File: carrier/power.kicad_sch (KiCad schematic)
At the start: 10 parts

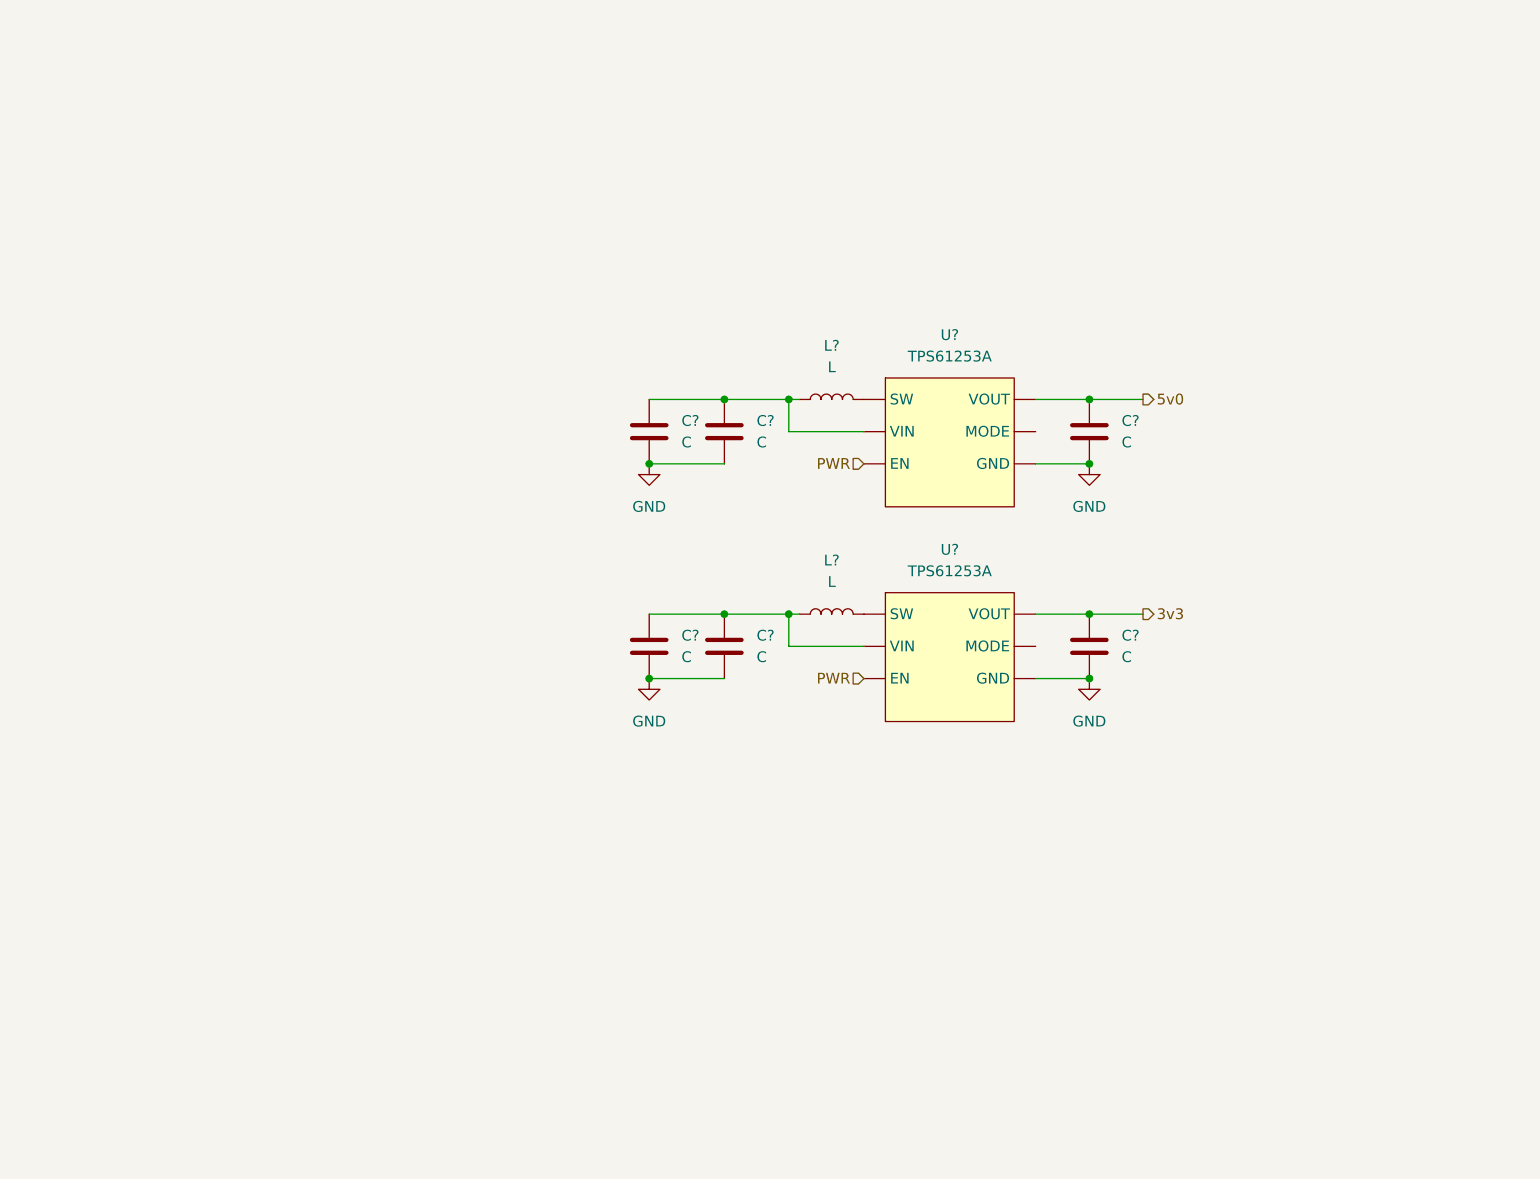
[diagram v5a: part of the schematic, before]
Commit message: add correct charge chip
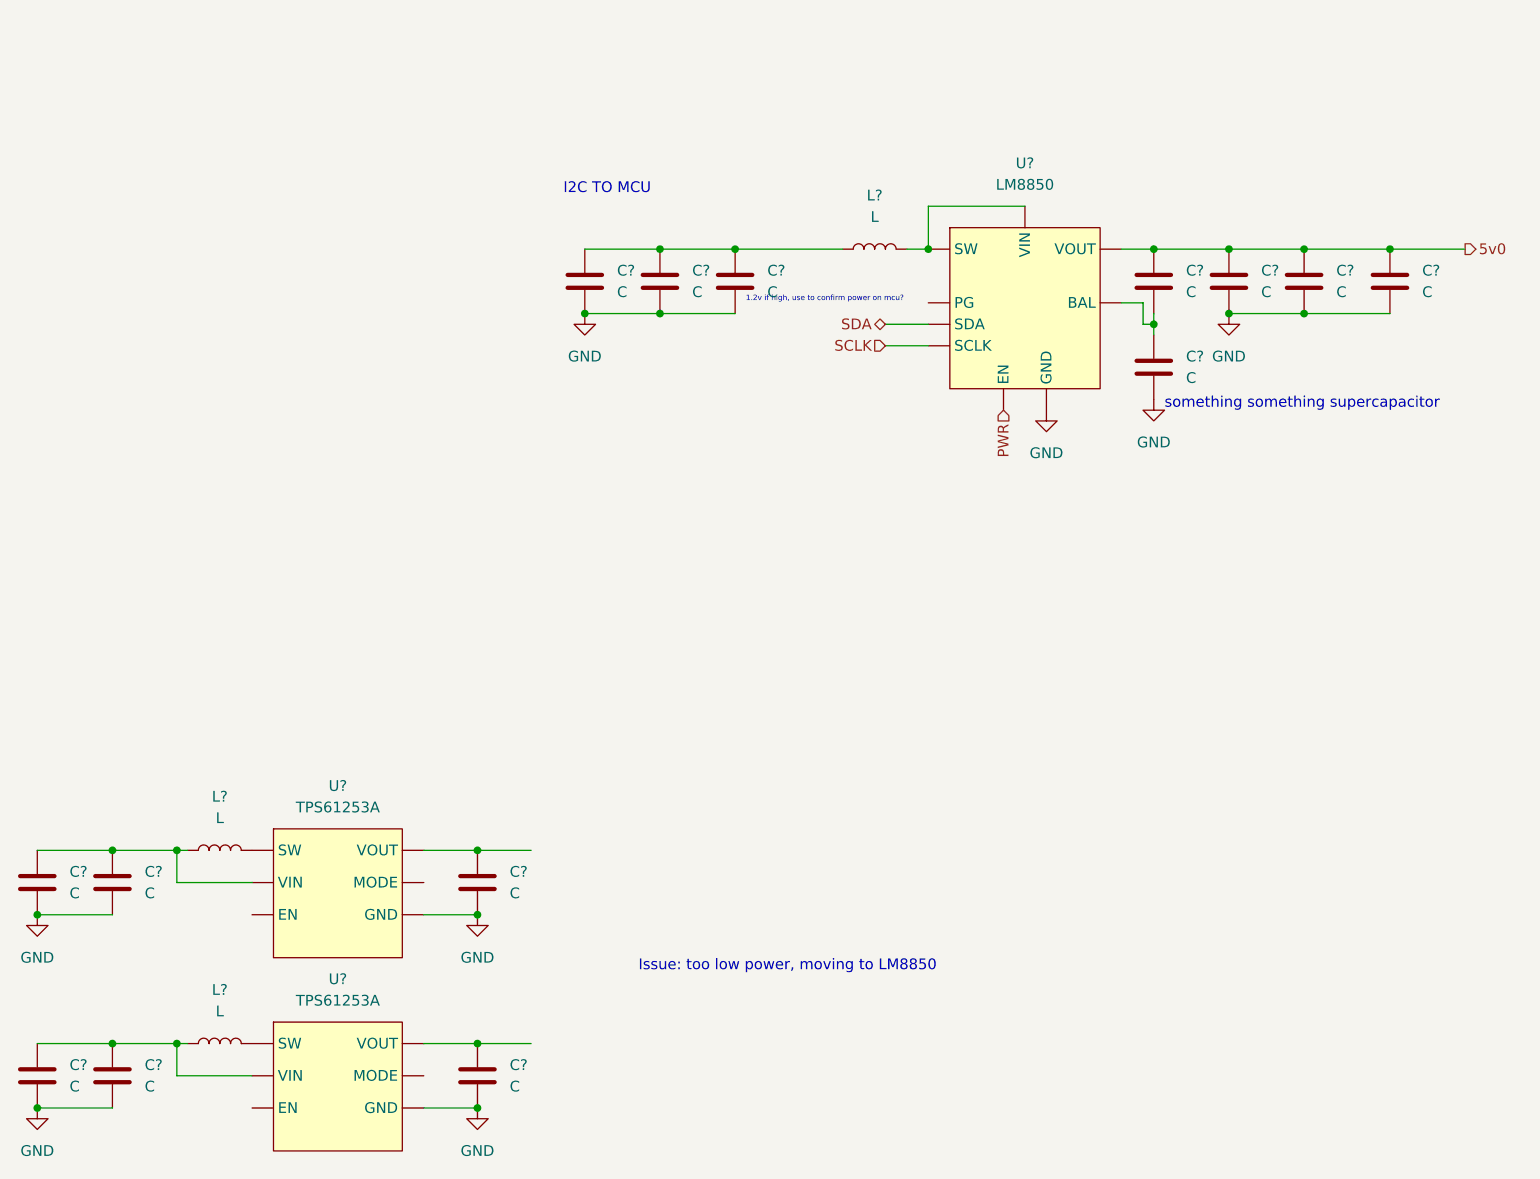
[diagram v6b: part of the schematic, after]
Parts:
- added C? (x8): C, symbol Device:C
- added L?: L, symbol Device:L
- added U?: LM8850, symbol CM4IO:LM8850
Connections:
- net 5v0: now also C?.1, C?.1, C?.1, C?.1, U?. (VOUT); no longer C?.1, U?. (VOUT)
- net GND: now also C?.2, C?.2, C?.2, C?.2, C?.2, C?.2, C?.2, U?. (VOUT)
- net PWR: now also U?. (VOUT); no longer U?. (VOUT), U?. (VOUT)
- net 3v3: no longer names the net of C?.1, U?. (VOUT)
- new net: C?.1, C?.2, U?. (VOUT)
- new net: C?.1, C?.1, C?.1, L?.1
- new net: L?.2, U?. (VOUT)
- new net: C?.1, U?. (VOUT)
- new net SCLK: U?. (VOUT)
- new net SDA: U?. (VOUT)
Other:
- note added: "1.2v if high, use to confirm power on mcu?"
- note added: "I2C TO MCU"
- note added: "Issue: too low power, moving to LM8850"
- note added: "something something supercapacitor"
- moved on the sheet: C?, L?, U?

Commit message: aa
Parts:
- removed C? (x8): C, symbol Device:C
- removed L?: L, symbol Device:L
- removed U?: LM8850, symbol CM4IO:LM8850
- added C19, C?: C, symbol Device:C
- added C20: 220n, symbol Device:C
- added C? (x4): 150u, symbol Device:C_Polarized
- added D?: D_Schottky, symbol Device:D_Schottky
- added L?: 1uH, symbol Device:L
- added R?: 2, symbol Device:R
- added R?: nc, symbol Device:R
- added U5: MAX1709, Package_SO:TSSOP-28-1EP_4.4x9.7mm_P0.65mm_EP2.85x6.7mm, symbol CM4IO:MAX1709
- gave numbers to parts that had none: 10
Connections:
- net 5v0: now also C?.1, C?.1, D?.1 (K)
- net GND: now also C19.2, C20.2, C?.2, C?.2, C?.2, C?.2, C?.2, R?.2, U5. (SS/LM)
- new net: D?.2 (A), L?.1, U5. (SS/LM)
- new net: C19.1, R?.1, U5. (SS/LM)
- new net: C?.1, R?.1, U5. (SS/LM)
- new net VBATT: C?.1, C?.1, L?.2, R?.2
- new net VREF: C20.1, U5. (SS/LM)
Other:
- note added: "'star' configuration, its like networking! meaning all ground points route to a single point"
- note added: "(reasoning: diode go righty - when voltage goes big this bokcs"
- note added: "alt: use max1708, but lower switch amperage is a bituneasy room wise."
- note added: "ferrite core"
- note added: "int. clock"
- note added: "note: not actual star, just all planes need to connect to one common connection. ie: analogue signals we have here should be in one section of the board, and then be routed to the same common ground point as digital often resolved by ground planes"
- note added: "regulator push button"
- note added: "resistor is for setting current limit. im not too fussed here for now, but might like to set this later."
- note added: "schorrkt sioswa uaws ro mKW XLmpws"
- note added: "schottky > silicon for lower drop and fast switching"
- note added: "shunt"
- note added: "tie ONB high and then toggle via ONA"
- note removed: "1.2v if high, use to confirm power on mcu?"
- note removed: "I2C TO MCU"
- note removed: "something something supercapacitor"
